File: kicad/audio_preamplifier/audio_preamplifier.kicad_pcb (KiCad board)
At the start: 2 copper layers, 33 parts, among them P1 CONN_6, P2 IN, P3 OUT, P4 POWER, U1 PIC12F629, U2 78L05, U3 TL072

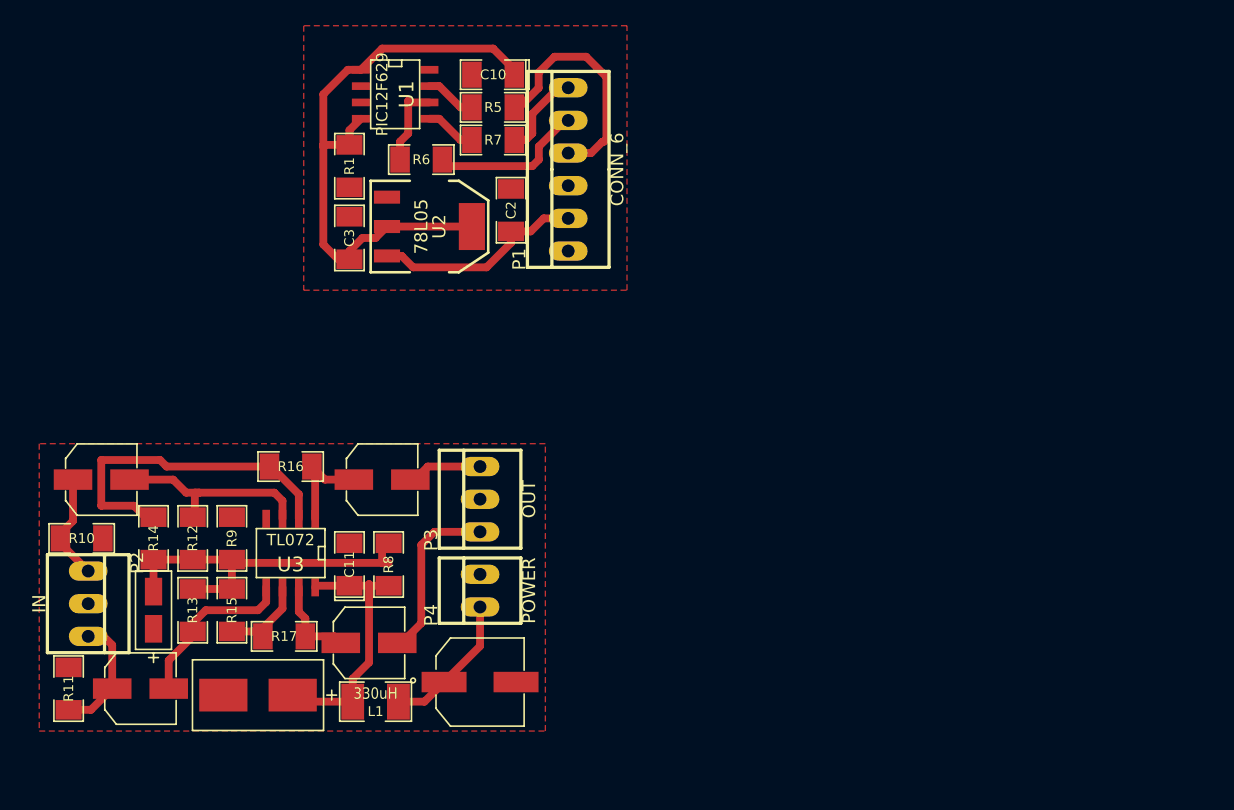
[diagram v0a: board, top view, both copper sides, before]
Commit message: new kicad version components in schematics
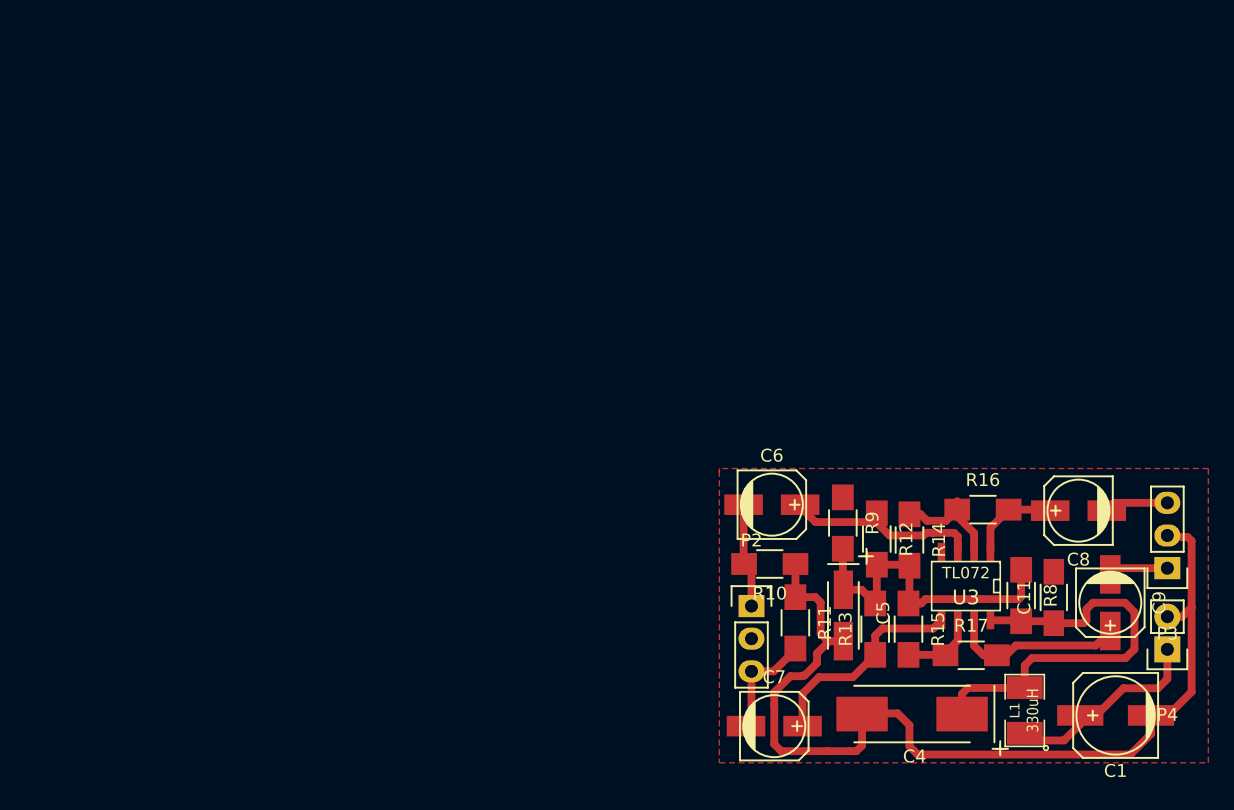
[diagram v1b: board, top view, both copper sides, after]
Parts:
- removed C10: 100n, SM1206POL
- removed C2, C3: 100n, SM1206
- removed P1: CONN_6, PINHEAD1-6
- removed R1: 10k, SM1206
- removed R5, R6, R7: 3k3, SM1206
- removed U1: PIC12F629, SO8E
- removed U2: 78L05, SOT223
- C1: value 100m -> 100m/25V; footprint c-smd-6.3mmx8mm -> Capacitors_SMD:c_elec_6.3x7.7
- C11: footprint SM1206POL -> Capacitors_SMD:C_1206_HandSoldering
- C4: value 47m -> 47m/25V; footprint TC-D-7343-31-A -> Capacitors_Tantalum_SMD:TantalC_SizeD_EIA-7343_HandSoldering
- C5: value 2m2 -> 2m2/16V; footprint TC-A-3216-18-A -> Capacitors_Tantalum_SMD:TantalC_SizeA_EIA-3216_HandSoldering
- C6, C7: value 10m -> 10m/16V; footprint c-smd-5mmx6.1mm -> Capacitors_SMD:c_elec_5x5.8
- C8, C9: value 47m -> 47m/25V; footprint c-smd-5mmx6.1mm -> Capacitors_SMD:c_elec_5x5.8
- P2: value IN -> CONN_01X03; footprint PINHEAD1-3 -> Pin_Headers:Pin_Header_Straight_1x03
- P3: value OUT -> CONN_01X03; footprint PINHEAD1-3 -> Pin_Headers:Pin_Header_Straight_1x03
- P4: value POWER -> CONN_01X02; footprint PINHEAD1-2 -> Pin_Headers:Pin_Header_Straight_1x02
- R10, R11, R12, R13, R14, R15, R16, R17, R8, R9: footprint SM1206 -> Resistors_SMD:R_1206_HandSoldering
- moved R14 58.8 mm to (197.0, 126.1)
- moved C9 57.7 mm to (212.6, 131.0), turned to 270 degrees
- moved R11 56.8 mm to (188.1, 132.6), turned to 270 degrees
- moved C11 54.8 mm to (208.2, 130.6)
- moved C8 54.2 mm to (210.1, 123.8), turned to 180 degrees
- moved R16 54.0 mm to (202.7, 123.7)
- moved P3 53.7 mm to (217.0, 128.3), turned to 180 degrees
- moved C5 53.7 mm to (191.8, 132.0), turned to 270 degrees
- moved P4 53.7 mm to (217.0, 134.6), turned to 180 degrees
- moved R10 53.6 mm to (186.1, 128.0)
- moved R17 53.5 mm to (201.8, 135.1)
- moved R12 53.2 mm to (194.4, 126.0)
- moved R13 53.1 mm to (194.3, 133.0), turned to 90 degrees
- moved R15 52.6 mm to (196.9, 133.0), turned to 270 degrees
- moved U3 52.6 mm to (201.4, 129.7)
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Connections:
- net N-000005 renamed /12V_filtered
- C5 pad 1: AGND -> /virtual_gnd
- C5 pad 2: N-000001 -> AGND
- C6 pad 1: right_in -> Net-(C6-Pad1)
- C6 pad 2: N-000025 -> right_in
- C7 pad 1: left_in -> Net-(C7-Pad1)
- C7 pad 2: N-000021 -> left_in
- R11 pad 1: left_in -> AGND
- R11 pad 2: AGND -> left_in
- R12 pad 1: N-000025 -> Net-(C6-Pad1)
- R12 pad 2: N-000001 -> /virtual_gnd
- R13 pad 1: N-000001 -> Net-(C7-Pad1)
- R13 pad 2: N-000021 -> /virtual_gnd
- R14 pad 2: N-000001 -> /virtual_gnd
- R15 pad 1: N-000018 -> /virtual_gnd
- R15 pad 2: N-000001 -> Net-(R15-Pad2)
- R17 pad 1: N-000018 -> Net-(R15-Pad2)
- R8 pad 1: N-000001 -> /virtual_gnd
- R9 pad 2: N-000001 -> /virtual_gnd
- U3 pad 3: N-000025 -> Net-(C6-Pad1)
- U3 pad 5: N-000021 -> Net-(C7-Pad1)
- U3 pad 6: N-000018 -> Net-(R15-Pad2)
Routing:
- net AGND: track 0.00 -> 80.2 mm
- net +5V: track 47.1 -> 0.00 mm
- net N-000001: track 28.0 -> 0.00 mm
- net /virtual_gnd: track 0.00 -> 26.0 mm
- net CLK: track 18.4 -> 0.00 mm
- net Net-(C7-Pad1): track 0.00 -> 16.9 mm
- net POWER_CTL: track 16.6 -> 0.00 mm
- net Net-(R14-Pad1): track 26.4 -> 9.86 mm
- net N-000025: track 16.3 -> 0.00 mm
- net Net-(C6-Pad1): track 0.00 -> 16.0 mm
- net /12V_filtered: track 20.4 -> 34.5 mm
- net N-000021: track 13.4 -> 0.00 mm
- net DataIn: track 12.1 -> 0.00 mm
- net left_out: track 13.6 -> 4.64 mm
- net Net-(C9-Pad1): track 6.99 -> 15.0 mm
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- removed copper zone on F.Cu, net GND

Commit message: fix values
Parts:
- removed P4: CONN_01X02, Pin_Headers:Pin_Header_Straight_1x02
- C11, C4, C5: moved to B.Cu
- P3: footprint Pin_Headers:Pin_Header_Straight_1x03 -> Pin_Headers:Pin_Header_Straight_1x05
- R10, R11, R12, R13, R14, R15, R16, R17, R8, R9: footprint Resistors_SMD:R_1206_HandSoldering -> Resistors_SMD:R_0805_HandSoldering; moved to B.Cu
- moved L1 13.3 mm to (192.8, 141.0), turned to 180 degrees
- moved C11 11.2 mm to (204.8, 141.3), turned to 0 degrees
- moved C6 10.6 mm to (193.5, 131.1)
- moved R9 10.2 mm to (200.0, 130.9)
- moved C1 9.94 mm to (203.1, 139.6)
- moved R12 9.77 mm to (202.9, 130.9)
- moved R14 9.24 mm to (204.9, 130.9)
- moved R13 8.96 mm to (202.9, 135.6)
- moved R16 8.66 mm to (207.5, 130.9), turned to 90 degrees
- moved R15 8.36 mm to (204.9, 135.6)
- moved C7 8.13 mm to (193.5, 136.6)
- moved R11 7.89 mm to (195.4, 135.6)
- moved R8 7.76 mm to (200.0, 135.7)
- moved C8 7.44 mm to (210.6, 131.3)
- moved R10 7.23 mm to (193.2, 129.5)
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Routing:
- net /virtual_gnd: track 26.0 -> 15.9 mm
- net AGND: track 80.2 -> 71.4 mm, vias 0 -> 5
- net /12V_filtered: track 34.5 -> 27.8 mm, vias 0 -> 2
- net Net-(C7-Pad1): track 16.9 -> 11.2 mm, vias 0 -> 1
- net Net-(C9-Pad1): track 15.0 -> 9.69 mm, vias 0 -> 1
- net +12V: track 15.6 -> 20.0 mm, vias 0 -> 1
- net Net-(R15-Pad2): track 6.00 -> 9.86 mm, vias 0 -> 1
- net Net-(R14-Pad1): track 9.86 -> 7.68 mm, vias 0 -> 1
- net Net-(C6-Pad1): track 16.0 -> 14.0 mm, vias 0 -> 2
- net right_in: track 8.14 -> 6.23 mm, vias 0 -> 1
- net Net-(C8-Pad1): track 7.13 -> 8.42 mm, vias 0 -> 1
- net left_out: track 4.64 -> 5.80 mm, vias 0 -> 2
- net left_in: track 8.67 -> 9.69 mm, vias 0 -> 1
- added copper zone on B.Cu, net AGND
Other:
- board outline added: 26.2 x 15 mm

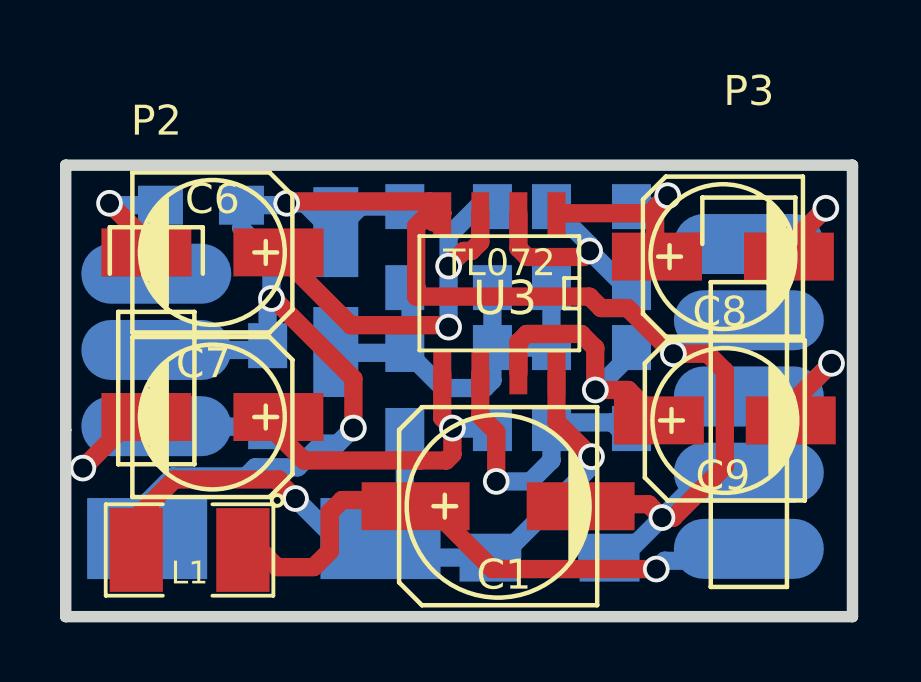
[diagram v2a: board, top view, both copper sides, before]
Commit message: assamble plan, BOM
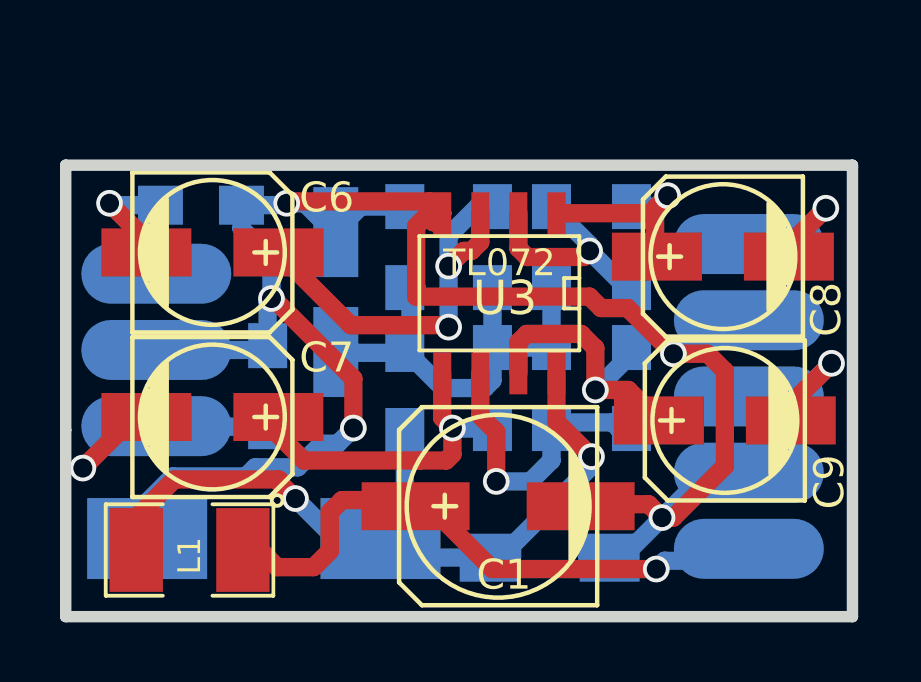
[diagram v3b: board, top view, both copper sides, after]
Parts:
- P2: footprint Pin_Headers:Pin_Header_Straight_1x03 -> modules:Pin_Header_Straight_1x03_no_silk
- P3: footprint Pin_Headers:Pin_Header_Straight_1x05 -> modules:Pin_Header_Straight_1x05_no_silk_screen
- R14, R15: value 330k -> 100k
- R16, R17: value 7M5 -> 2M2
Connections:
- P3 pad 1: left_out -> right_out
- P3 pad 3: right_out -> left_out
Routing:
- net right_out: track 5.20 -> 5.45 mm, vias 0 -> 1
- net left_out: track 5.80 -> 5.54 mm, vias 2 -> 1
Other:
- board text added: "+12V"
- board text added: "GND"
- board text added: "L-IN"
- board text added: "L-OUT"
- board text added: "R-IN"
- board text added: "R-OUT"
